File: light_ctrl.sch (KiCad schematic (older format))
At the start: 26 parts, among them J5 Conn_01x08, Q1 DMG3406L, Q2 DMG3406L, Q3 DMG3406L, Q4 DMG3406L, Q5 DMG3406L

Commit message: layout
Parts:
- added C5: 100nF, Capacitor_SMD:C_0805_2012Metric_Pad1.15x1.40mm_HandSolder, symbol Device:C
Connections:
- net labels added: +3.3V
- wire segments 62 -> 67
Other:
- note added: "Setup I - close jumpers for external mosfets\nSetup II - mosfets on board"
- note removed: "Setup I ) close jumpers for external mosfets\nSetup II ) mosfets on board"
- moved on the sheet: J5, JP1, JP2, JP3, JP4, JP5, Q1, Q2, Q3, Q4, Q5, R10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

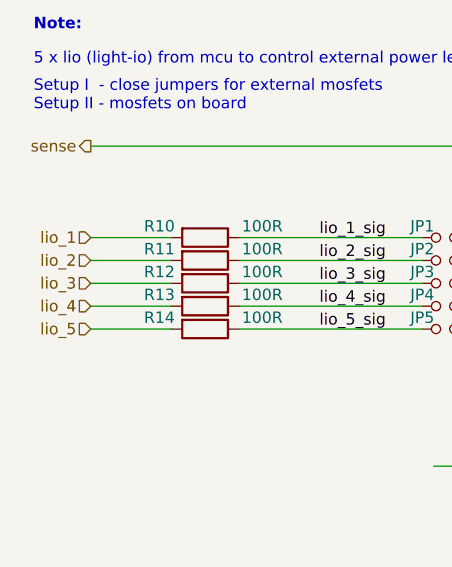
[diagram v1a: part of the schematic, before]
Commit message: added more circuit parts + new step files
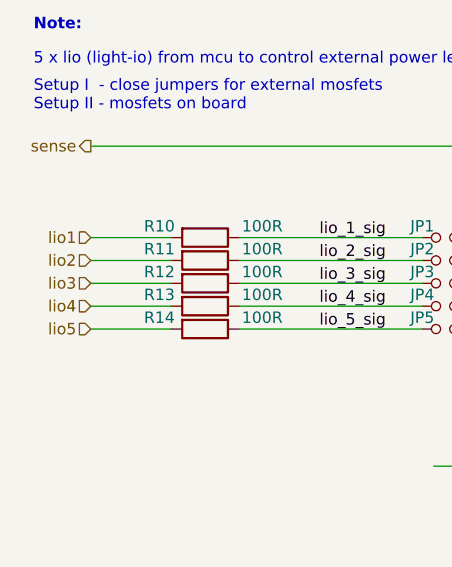
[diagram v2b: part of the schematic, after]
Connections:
- net labels added: lio1, lio2, lio3, lio4, lio5
- net labels removed: lio_1, lio_2, lio_3, lio_4, lio_5
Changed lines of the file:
@@
 $Descr A4 11693 8268
 encoding utf-8
-Sheet 5 5
+Sheet 4 6
 Title ""
 Date ""
@@
 $EndComp
 Text HLabel 1100 2200 0    50   Input ~ 0
-lio_2
+lio2
 Text HLabel 1100 2300 0    50   Input ~ 0
-lio_3
+lio3
 Text HLabel 1100 2400 0    50   Input ~ 0
-lio_4
+lio4
 Text HLabel 1100 2500 0    50   Input ~ 0
-lio_5
+lio5
 Text Notes 850  1350 0    50   ~ 0
 5 x lio (light-io) from mcu to control external power leds via pwm
@@
 Note:
 Text HLabel 1100 2100 0    50   Input ~ 0
-lio_1
+lio1
 Wire Wire Line
 	1450 2100 1100 2100

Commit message: started pcb routing
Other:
- note added: "Setup I ) close jumpers for external mosfets\nSetup II) mosfets on board | default"
- note removed: "Setup I - close jumpers for external mosfets\nSetup II - mosfets on board"
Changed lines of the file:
@@
 P 3750 3850
 F 0 "Q2" H 3954 3896 50  0000 L CNN
-F 1 "DMG3406L" H 3954 3805 50  0000 L CNN
+F 1 "DMG3406L" H 3370 3710 50  0000 L CNN
 F 2 "Package_TO_SOT_SMD:SOT-23" H 3950 3775 50  0001 L CIN
 F 3 "http://www.diodes.com/assets/Datasheets/DMG3406L.pdf" H 3750 3850 50  0001 L CNN
@@
 P 3950 4700
 F 0 "Q3" H 4154 4746 50  0000 L CNN
-F 1 "DMG3406L" H 4154 4655 50  0000 L CNN
+F 1 "DMG3406L" H 3580 4550 50  0000 L CNN
 F 2 "Package_TO_SOT_SMD:SOT-23" H 4150 4625 50  0001 L CIN
 F 3 "http://www.diodes.com/assets/Datasheets/DMG3406L.pdf" H 3950 4700 50  0001 L CNN
@@
 P 4150 5450
 F 0 "Q4" H 4354 5496 50  0000 L CNN
-F 1 "DMG3406L" H 4354 5405 50  0000 L CNN
+F 1 "DMG3406L" H 3760 5280 50  0000 L CNN
 F 2 "Package_TO_SOT_SMD:SOT-23" H 4350 5375 50  0001 L CIN
 F 3 "http://www.diodes.com/assets/Datasheets/DMG3406L.pdf" H 4150 5450 50  0001 L CNN
@@
 P 4350 6200
 F 0 "Q5" H 4554 6246 50  0000 L CNN
-F 1 "DMG3406L" H 4554 6155 50  0000 L CNN
+F 1 "DMG3406L" H 3980 6030 50  0000 L CNN
 F 2 "Package_TO_SOT_SMD:SOT-23" H 4550 6125 50  0001 L CIN
 F 3 "http://www.diodes.com/assets/Datasheets/DMG3406L.pdf" H 4350 6200 50  0001 L CNN
@@
 P 3550 3100
 F 0 "Q1" H 3754 3146 50  0000 L CNN
-F 1 "DMG3406L" H 3754 3055 50  0000 L CNN
+F 1 "DMG3406L" H 3180 2930 50  0000 L CNN
 F 2 "Package_TO_SOT_SMD:SOT-23" H 3750 3025 50  0001 L CIN
 F 3 "http://www.diodes.com/assets/Datasheets/DMG3406L.pdf" H 3550 3100 50  0001 L CNN
@@
 	4650 1800 4750 1800
 Text Notes 850  1550 0    50   ~ 0
-Setup I  - close jumpers for external mosfets\nSetup II - mosfets on board
+Setup I ) close jumpers for external mosfets\nSetup II) mosfets on board | default
 $Comp
 L Device:Jumper_NO_Small JP2

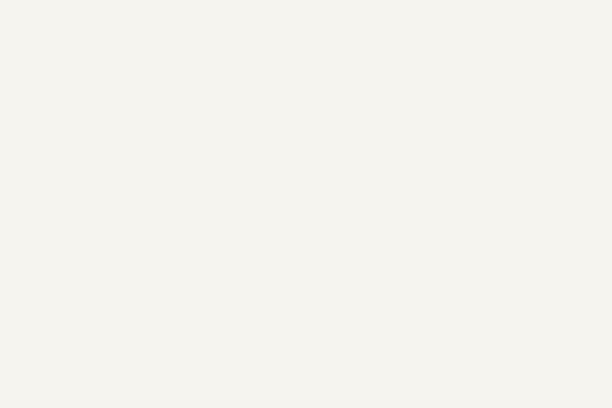
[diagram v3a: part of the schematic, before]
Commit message: layout and more silk informations
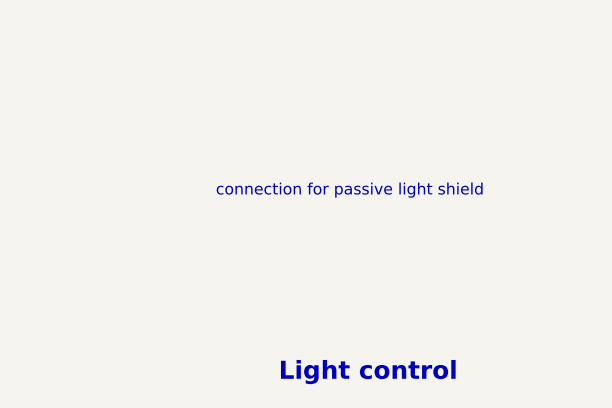
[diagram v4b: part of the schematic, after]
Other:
- note added: "Light control"
- note added: "connection for passive light shield"
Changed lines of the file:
@@
 Wire Wire Line
 	4650 1350 4650 1600
+Text Notes 7325 7510 0    79   ~ 16
+Light control
+Text Notes 7050 6700 0    50   ~ 0
+connection for passive light shield
 $EndSCHEMATC

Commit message: finished layout, created production files and added readme
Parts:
- C5: LCSC (none) -> C28233; MPN (none) -> CL21B104KCFNNNE
- J5: footprint Connector_PinHeader_2.54mm:PinHeader_1x10_P2.54mm_Vertical -> Custom:LED_shield
- Q1, Q2, Q3, Q4, Q5: LCSC (none) -> C154722; MPN (none) -> DMG3420U-7
- R10, R11, R12, R13, R14: LCSC (none) -> C17408; MPN (none) -> 0805W8F1000T5E
- R15, R16, R17, R19, R21: LCSC (none) -> C17407; MPN (none) -> 0805W8F1003T5E
- R18, R20, R22, R23, R24: LCSC (none) -> C21355; MPN (none) -> 1210W3F500LT5E
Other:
- note added: "1.0"
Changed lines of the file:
@@
 F 2 "Resistor_SMD:R_0805_2012Metric_Pad1.15x1.40mm_HandSolder" V 3230 4000 50  0001 C CNN
 F 3 "~" H 3300 4000 50  0001 C CNN
+F 4 "0805W8F1003T5E" H 3300 4000 50  0001 C CNN "MPN"
+F 5 "C17407" H 3300 4000 50  0001 C CNN "LCSC"
 	1    3300 4000
 	1    0    0    -1
@@
 F 2 "Package_TO_SOT_SMD:SOT-23" H 3950 3775 50  0001 L CIN
 F 3 "http://www.diodes.com/assets/Datasheets/DMG3406L.pdf" H 3750 3850 50  0001 L CNN
+F 4 "DMG3420U-7" H 3750 3850 50  0001 C CNN "MPN"
+F 5 "C154722" H 3750 3850 50  0001 C CNN "LCSC"
 	1    3750 3850
 	1    0    0    -1
@@
 F 2 "Resistor_SMD:R_0805_2012Metric_Pad1.15x1.40mm_HandSolder" V 1530 2100 50  0001 C CNN
 F 3 "~" H 1600 2100 50  0001 C CNN
+F 4 "0805W8F1000T5E" H 1600 2100 50  0001 C CNN "MPN"
+F 5 "C17408" H 1600 2100 50  0001 C CNN "LCSC"
 	1    1600 2100
 	0    1    1    0
@@
 F 2 "Resistor_SMD:R_0805_2012Metric_Pad1.15x1.40mm_HandSolder" V 1530 2200 50  0001 C CNN
 F 3 "~" H 1600 2200 50  0001 C CNN
+F 4 "0805W8F1000T5E" H 1600 2200 50  0001 C CNN "MPN"
+F 5 "C17408" H 1600 2200 50  0001 C CNN "LCSC"
 	1    1600 2200
 	0    1    1    0
@@
 F 2 "Resistor_SMD:R_0805_2012Metric_Pad1.15x1.40mm_HandSolder" V 1530 2300 50  0001 C CNN
 F 3 "~" H 1600 2300 50  0001 C CNN
+F 4 "0805W8F1000T5E" H 1600 2300 50  0001 C CNN "MPN"
+F 5 "C17408" H 1600 2300 50  0001 C CNN "LCSC"
 	1    1600 2300
 	0    1    1    0
@@
 F 2 "Resistor_SMD:R_0805_2012Metric_Pad1.15x1.40mm_HandSolder" V 1530 2400 50  0001 C CNN
 F 3 "~" H 1600 2400 50  0001 C CNN
+F 4 "0805W8F1000T5E" H 1600 2400 50  0001 C CNN "MPN"
+F 5 "C17408" H 1600 2400 50  0001 C CNN "LCSC"
 	1    1600 2400
 	0    1    1    0
@@
 F 2 "Resistor_SMD:R_0805_2012Metric_Pad1.15x1.40mm_HandSolder" V 1530 2500 50  0001 C CNN
 F 3 "~" H 1600 2500 50  0001 C CNN
+F 4 "0805W8F1000T5E" H 1600 2500 50  0001 C CNN "MPN"
+F 5 "C17408" H 1600 2500 50  0001 C CNN "LCSC"
 	1    1600 2500
 	0    1    1    0
@@
 F 2 "Resistor_SMD:R_0805_2012Metric_Pad1.15x1.40mm_HandSolder" V 3430 4850 50  0001 C CNN
 F 3 "~" H 3500 4850 50  0001 C CNN
+F 4 "0805W8F1003T5E" H 3500 4850 50  0001 C CNN "MPN"
+F 5 "C17407" H 3500 4850 50  0001 C CNN "LCSC"
 	1    3500 4850
 	1    0    0    -1
@@
 F 2 "Package_TO_SOT_SMD:SOT-23" H 4150 4625 50  0001 L CIN
 F 3 "http://www.diodes.com/assets/Datasheets/DMG3406L.pdf" H 3950 4700 50  0001 L CNN
+F 4 "DMG3420U-7" H 3950 4700 50  0001 C CNN "MPN"
+F 5 "C154722" H 3950 4700 50  0001 C CNN "LCSC"
 	1    3950 4700
 	1    0    0    -1
@@
 F 2 "Resistor_SMD:R_0805_2012Metric_Pad1.15x1.40mm_HandSolder" V 3630 5600 50  0001 C CNN
 F 3 "~" H 3700 5600 50  0001 C CNN
+F 4 "0805W8F1003T5E" H 3700 5600 50  0001 C CNN "MPN"
+F 5 "C17407" H 3700 5600 50  0001 C CNN "LCSC"
 	1    3700 5600
 	1    0    0    -1
@@
 F 2 "Package_TO_SOT_SMD:SOT-23" H 4350 5375 50  0001 L CIN
 F 3 "http://www.diodes.com/assets/Datasheets/DMG3406L.pdf" H 4150 5450 50  0001 L CNN
+F 4 "DMG3420U-7" H 4150 5450 50  0001 C CNN "MPN"
+F 5 "C154722" H 4150 5450 50  0001 C CNN "LCSC"
 	1    4150 5450
 	1    0    0    -1
@@
 F 2 "Resistor_SMD:R_0805_2012Metric_Pad1.15x1.40mm_HandSolder" V 3830 6350 50  0001 C CNN
 F 3 "~" H 3900 6350 50  0001 C CNN
+F 4 "0805W8F1003T5E" H 3900 6350 50  0001 C CNN "MPN"
+F 5 "C17407" H 3900 6350 50  0001 C CNN "LCSC"
 	1    3900 6350
 	1    0    0    -1
@@
 F 2 "Package_TO_SOT_SMD:SOT-23" H 4550 6125 50  0001 L CIN
 F 3 "http://www.diodes.com/assets/Datasheets/DMG3406L.pdf" H 4350 6200 50  0001 L CNN
+F 4 "DMG3420U-7" H 4350 6200 50  0001 C CNN "MPN"
+F 5 "C154722" H 4350 6200 50  0001 C CNN "LCSC"
 	1    4350 6200
 	1    0    0    -1
@@
 F 2 "Resistor_SMD:R_0805_2012Metric_Pad1.15x1.40mm_HandSolder" V 3030 3250 50  0001 C CNN
 F 3 "~" H 3100 3250 50  0001 C CNN
+F 4 "0805W8F1003T5E" H 3100 3250 50  0001 C CNN "MPN"
+F 5 "C17407" H 3100 3250 50  0001 C CNN "LCSC"
 	1    3100 3250
 	1    0    0    -1
@@
 F 2 "Package_TO_SOT_SMD:SOT-23" H 3750 3025 50  0001 L CIN
 F 3 "http://www.diodes.com/assets/Datasheets/DMG3406L.pdf" H 3550 3100 50  0001 L CNN
+F 4 "DMG3420U-7" H 3550 3100 50  0001 C CNN "MPN"
+F 5 "C154722" H 3550 3100 50  0001 C CNN "LCSC"
 	1    3550 3100
 	1    0    0    -1
@@
 F 2 "Resistor_SMD:R_1210_3225Metric_Pad1.42x2.65mm_HandSolder" V 4380 5750 50  0001 C CNN
 F 3 "~" H 4450 5750 50  0001 C CNN
+F 4 "1210W3F500LT5E" H 4450 5750 50  0001 C CNN "MPN"
+F 5 "C21355" H 4450 5750 50  0001 C CNN "LCSC"
 	1    4450 5750
 	1    0    0    -1
@@
 F 2 "Resistor_SMD:R_1210_3225Metric_Pad1.42x2.65mm_HandSolder" V 4180 5000 50  0001 C CNN
 F 3 "~" H 4250 5000 50  0001 C CNN
+F 4 "1210W3F500LT5E" H 4250 5000 50  0001 C CNN "MPN"
+F 5 "C21355" H 4250 5000 50  0001 C CNN "LCSC"
 	1    4250 5000
 	1    0    0    -1
@@
 F 2 "Resistor_SMD:R_1210_3225Metric_Pad1.42x2.65mm_HandSolder" V 3980 4250 50  0001 C CNN
 F 3 "~" H 4050 4250 50  0001 C CNN
+F 4 "1210W3F500LT5E" H 4050 4250 50  0001 C CNN "MPN"
+F 5 "C21355" H 4050 4250 50  0001 C CNN "LCSC"
 	1    4050 4250
 	1    0    0    -1
@@
 F 2 "Resistor_SMD:R_1210_3225Metric_Pad1.42x2.65mm_HandSolder" V 3780 3400 50  0001 C CNN
 F 3 "~" H 3850 3400 50  0001 C CNN
+F 4 "1210W3F500LT5E" H 3850 3400 50  0001 C CNN "MPN"
+F 5 "C21355" H 3850 3400 50  0001 C CNN "LCSC"
 	1    3850 3400
 	1    0    0    -1
@@
 F 2 "Resistor_SMD:R_1210_3225Metric_Pad1.42x2.65mm_HandSolder" V 3580 2700 50  0001 C CNN
 F 3 "~" H 3650 2700 50  0001 C CNN
+F 4 "1210W3F500LT5E" H 3650 2700 50  0001 C CNN "MPN"
+F 5 "C21355" H 3650 2700 50  0001 C CNN "LCSC"
 	1    3650 2700
 	1    0    0    -1
@@
 F 0 "J5" H 5030 1992 50  0000 L CNN
 F 1 "Conn_01x08" H 5030 1901 50  0000 L CNN
-F 2 "Connector_PinHeader_2.54mm:PinHeader_1x10_P2.54mm_Vertical" H 4950 2000 50  0001 C CNN
+F 2 "Custom:LED_shield" H 4950 2000 50  0001 C CNN
 F 3 "~" H 4950 2000 50  0001 C CNN
 	1    4950 2000
@@
 F 2 "Capacitor_SMD:C_0805_2012Metric_Pad1.15x1.40mm_HandSolder" H 4988 1200 50  0001 C CNN
 F 3 "~" H 4950 1350 50  0001 C CNN
+F 4 "CL21B104KCFNNNE" H 4950 1350 50  0001 C CNN "MPN"
+F 5 "C28233" H 4950 1350 50  0001 C CNN "LCSC"
 	1    4950 1350
 	0    -1   -1   0
@@
 Text Notes 7050 6700 0    50   ~ 0
 connection for passive light shield
+Text Notes 10600 7640 0    50   ~ 0
+1.0
 $EndSCHEMATC
